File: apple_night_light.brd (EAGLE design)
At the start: 100 x 55 mm, 46 parts, among them Y1 16MHZ, Y2 16mhz

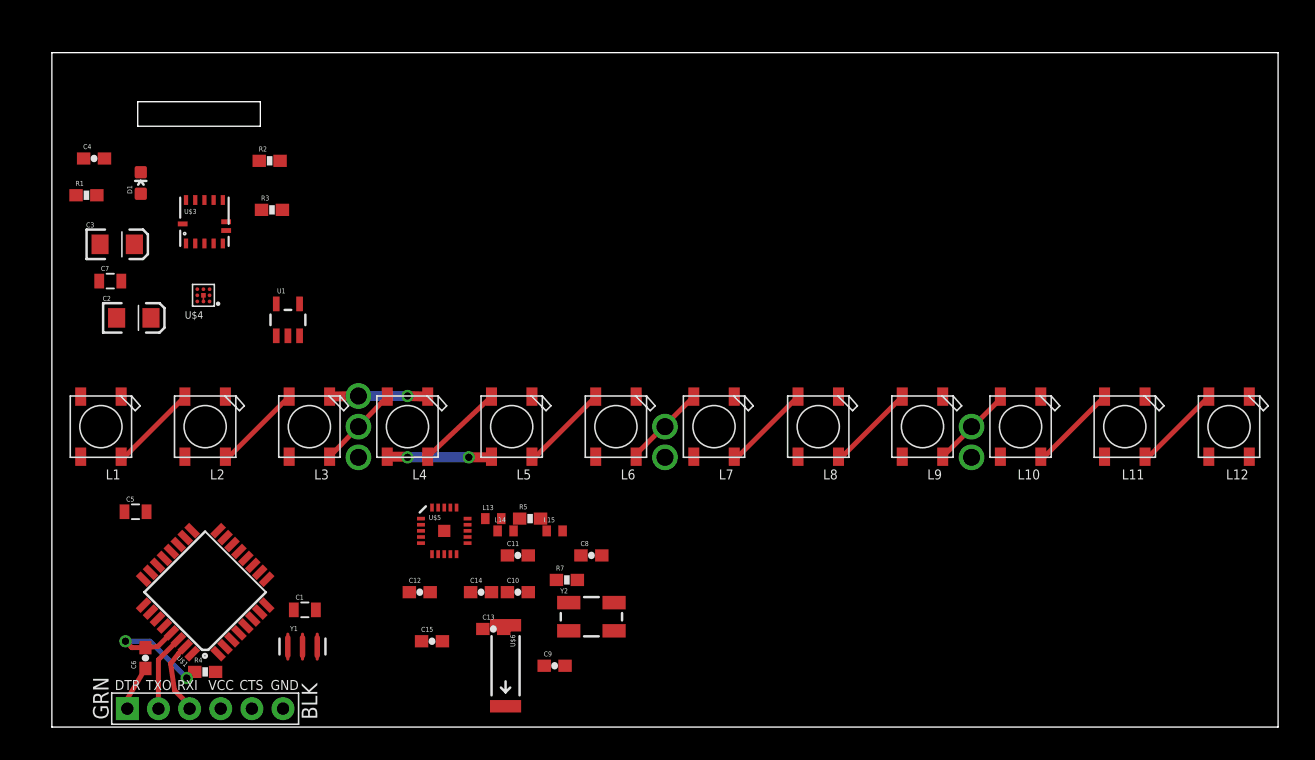
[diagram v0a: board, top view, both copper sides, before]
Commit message: some routing, adding current sensor, ground pours
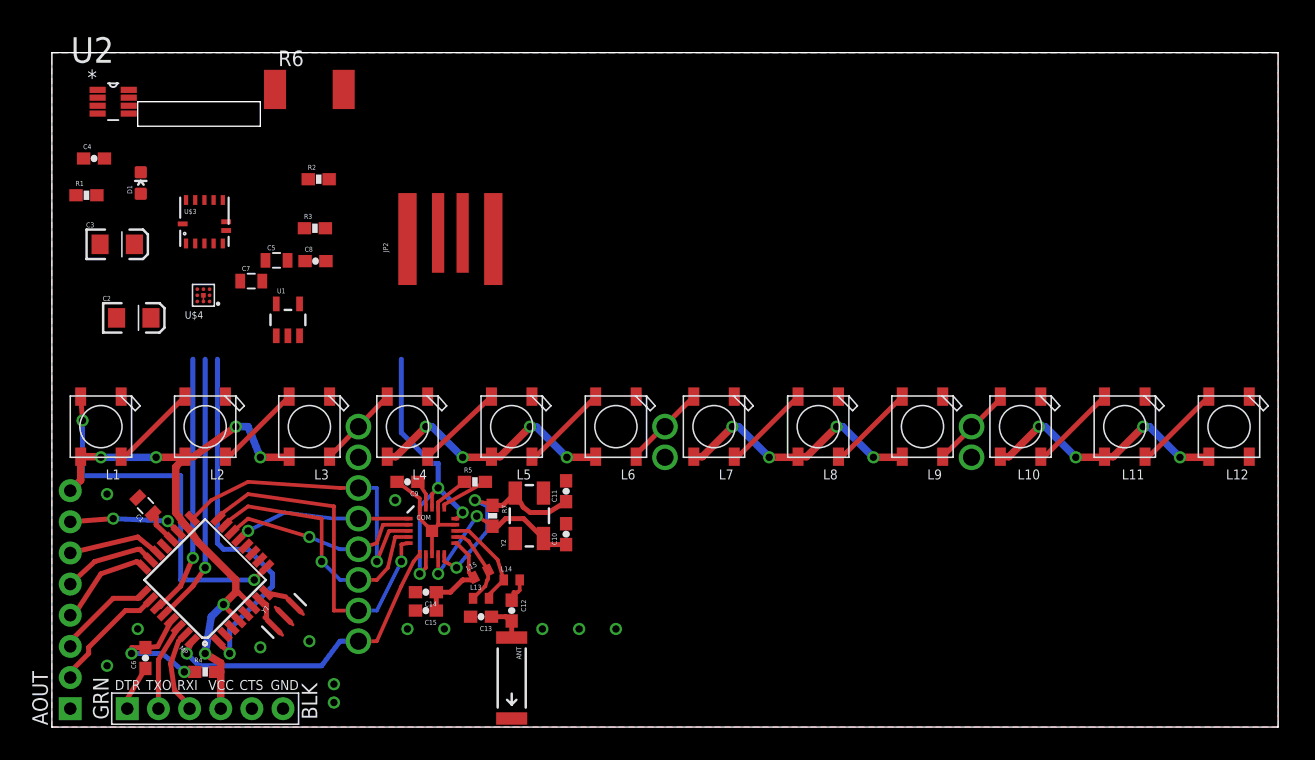
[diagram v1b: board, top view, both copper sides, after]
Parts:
- removed U$1: AVR-MEGA8-AI, SparkFun-DigitalIC:TQFP32-08
- removed U$5: NRF24L01SMD, SparkFun-RF:QFN20
- removed U$6: ANTENNA2SMD5, SparkFun-RF:ANTENNA-CHIP5
- added ANT: ANTENNA2SMD5, SparkFun-RF:ANTENNA-CHIP5
- added AOUT: (no value), SparkFun-Connectors:1X08_PIN1_NO_SILK
- added COM: NRF24L01SMD, SparkFun-RF:QFN20
- added JP2: USBPCB, SparkFun-Connectors:USB-A-PCB
- added MP: AVR-MEGA8-AI, SparkFun-DigitalIC:TQFP32-08
- added R6: 0.1/1% (PT2512FK-070R1L), SparkFun-Resistors:R2512
- added U2: INA219AIDCNR, Texas Instruments_By_element14_Batch_1:SOT65P280X145-8N
- moved C8 32.9 mm to (21.5, 38.0)
- moved C5 23.5 mm to (18.3, 38.1)
- moved C9 19.2 mm to (29.0, 20.0), turned to 180 degrees
- moved C1 15.5 mm to (7.63, 18.1), turned to 133.6 degrees
- moved C7 11.5 mm to (16.3, 36.4)
- moved Y2 9.66 mm to (38.9, 17.2), turned to 90 degrees
- moved R7 8.01 mm to (35.9, 17.2), turned to 270 degrees
- moved C12 7.65 mm to (37.5, 9.50), turned to 270 degrees
- moved L15 6.95 mm to (35.0, 12.5), turned to 26.5 degrees
- moved L13 6.58 mm to (35.0, 10.5)
- moved C11 6.55 mm to (41.9, 19.2), turned to 90 degrees
- moved C10 6.16 mm to (41.9, 15.7), turned to 90 degrees
- moved R5 5.41 mm to (34.5, 20.0)
- moved C14 4.50 mm to (30.5, 11.0), turned to 180 degrees
- moved R2 4.27 mm to (21.8, 44.7)
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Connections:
- removed net D5: U$1.9
- new net D4: MP.2
- net +3V3: now also COM.15, COM.18, COM.7; no longer R2.2, R3.2, U$5.15, U$5.18, U$5.7
- net +5V: now also AOUT.8, JP2.5V, MP.18, MP.4, MP.6, R2.2, R3.2, R6.2, U2.1, U2.4; no longer U$1.18, U$1.4, U$1.6
- net A0: now also AOUT.5, MP.23; no longer U$1.23
- net A1: now also AOUT.4, MP.24; no longer U$1.24
- net A2: now also AOUT.3, MP.25; no longer U$1.25
- net A3: now also AOUT.2, MP.26; no longer U$1.26
- net A6: now also AOUT.7, MP.19; no longer U$1.19
- net A7: now also AOUT.6, MP.22; no longer U$1.22
- net CE: now also COM.1, MP.13; no longer U$1.13, U$5.1
- net CSN: now also COM.2, MP.14; no longer U$1.14, U$5.2
- net D6: now also MP.10; no longer U$1.10
- net D7: now also MP.11; no longer U$1.11
- net D8: now also MP.12; no longer U$1.12
- net GND: now also AOUT.1, COM.0, COM.14, COM.17, COM.20, COM.8, JP2.GND, MP.21, MP.3, MP.5, R6.1, U2.2, U2.3; no longer U$1.21, U$1.3, U$1.5, U$5.0, U$5.14, U$5.17, U$5.20, U$5.8
- net IRQ: now also COM.6, MP.32; no longer U$1.32, U$5.6
- net MISO: now also COM.5, MP.16; no longer U$1.16, U$5.5
- net MOSI: now also COM.4, MP.15; no longer U$1.15, U$5.4
- net N$1: now also COM.11; no longer U$5.11
- net N$10: now also MP.7; no longer U$1.7
- net N$15: now also COM.19; no longer U$5.19
- net N$22: now also MP.29; no longer U$1.29
- net N$26: now also COM.13; no longer U$5.13
- net N$27: now also COM.9; no longer U$5.9
- net N$30: now also COM.10; no longer U$5.10
- net N$32: now also ANT.FEED; no longer U$6.FEED
- net N$6: now also COM.12; no longer U$5.12
- net N$7: now also MP.20; no longer U$1.20
- net N$8: now also COM.16; no longer U$5.16
- net N$9: now also MP.8; no longer U$1.8
- net NPIN: now also MP.9; no longer U$1.2
- net PROXINT: now also MP.1
- net RXI: now also MP.30; no longer U$1.30
- net SCK: now also COM.3, MP.17; no longer U$1.17, U$5.3
- net SCL: now also MP.28, U2.5; no longer U$1.28
- net SDA: now also MP.27, U2.6
- net TXO: now also MP.31; no longer U$1.31
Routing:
- net +5V: track 8.60 -> 114.5 mm, vias 2 -> 18
- net NPIN: track 0.00 -> 30.4 mm, vias 0 -> 2
- net PROXINT: track 0.00 -> 29.9 mm, vias 0 -> 1
- net MISO: track 0.00 -> 28.7 mm, vias 0 -> 2
- net +3V3: track 0.00 -> 26.9 mm, vias 0 -> 3
- net SCK: track 0.00 -> 26.3 mm, vias 0 -> 2
- net IRQ: track 0.00 -> 25.9 mm, vias 0 -> 2
- net MOSI: track 0.00 -> 22.2 mm, vias 0 -> 2
- net SCL: track 0.00 -> 22.1 mm, vias 0 -> 1
- net SDA: track 0.00 -> 21.3 mm, vias 0 -> 1
- net N$30: track 0.00 -> 18.3 mm, vias 0 -> 2
- net CSN: track 0.00 -> 16.4 mm, vias 0 -> 2
- net N$27: track 0.00 -> 16.0 mm, vias 0 -> 2
- net CE: track 0.00 -> 14.5 mm, vias 0 -> 2
- net A3: track 0.00 -> 9.74 mm
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- added copper zone on layer 1, net GND
- added copper zone on layer 16, net GND

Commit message: usb passthrough placed, better routing on neopixel power
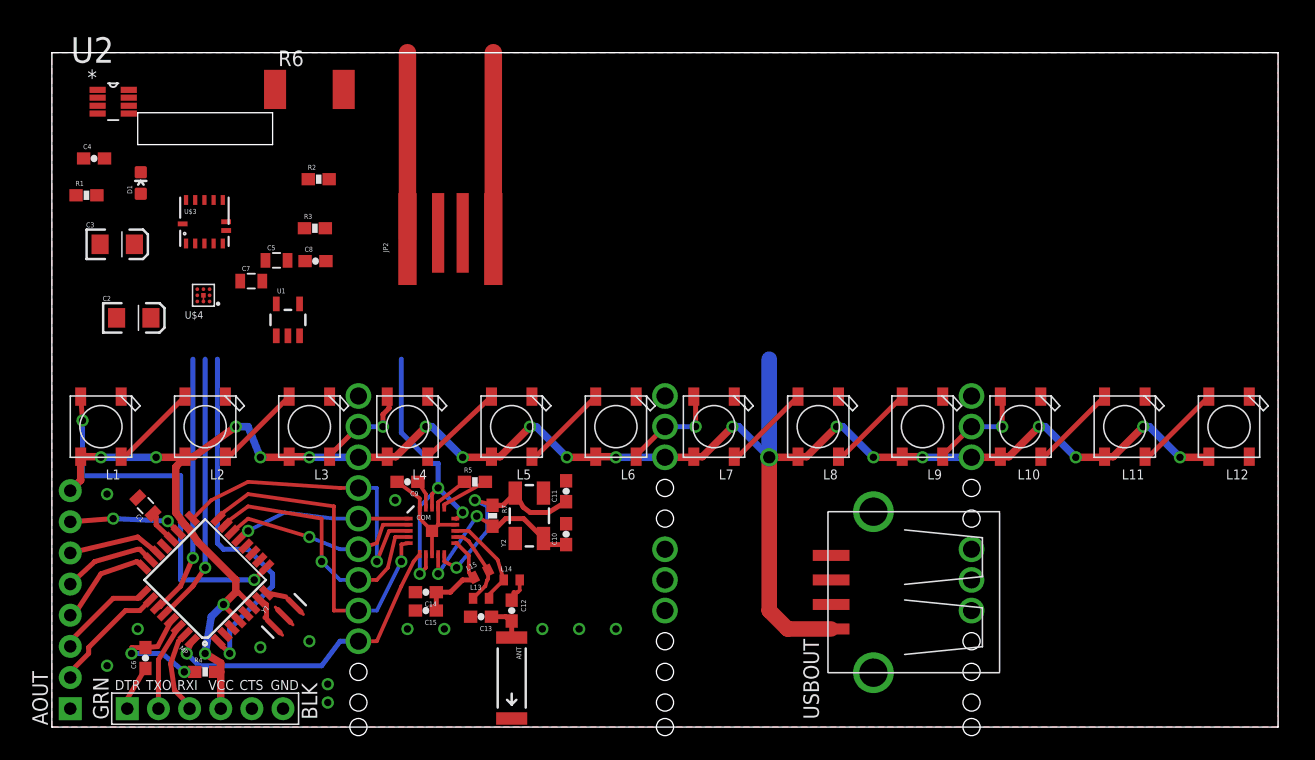
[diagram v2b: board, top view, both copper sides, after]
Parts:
- added USBOUT: USB-A-S, SparkFun-Connectors:USB-A-S
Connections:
- net +5V: now also USBOUT.VBUS
- net GND: now also USBOUT.GND
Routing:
- net +5V: track 114.5 -> 180.2 mm, vias 18 -> 24
- net GND: track 14.0 -> 29.2 mm, vias 13 -> 22
- net N$17: track 6.85 -> 8.64 mm, vias 0 -> 2
- net N$12: track 6.85 -> 8.49 mm, vias 0 -> 2
- net N$23: track 6.79 -> 8.14 mm, vias 0 -> 2
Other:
- outline, holes or cut-outs redrawn

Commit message: moved and corrected currentsensor, trying to fix clearances, adding temp/humidity sensor
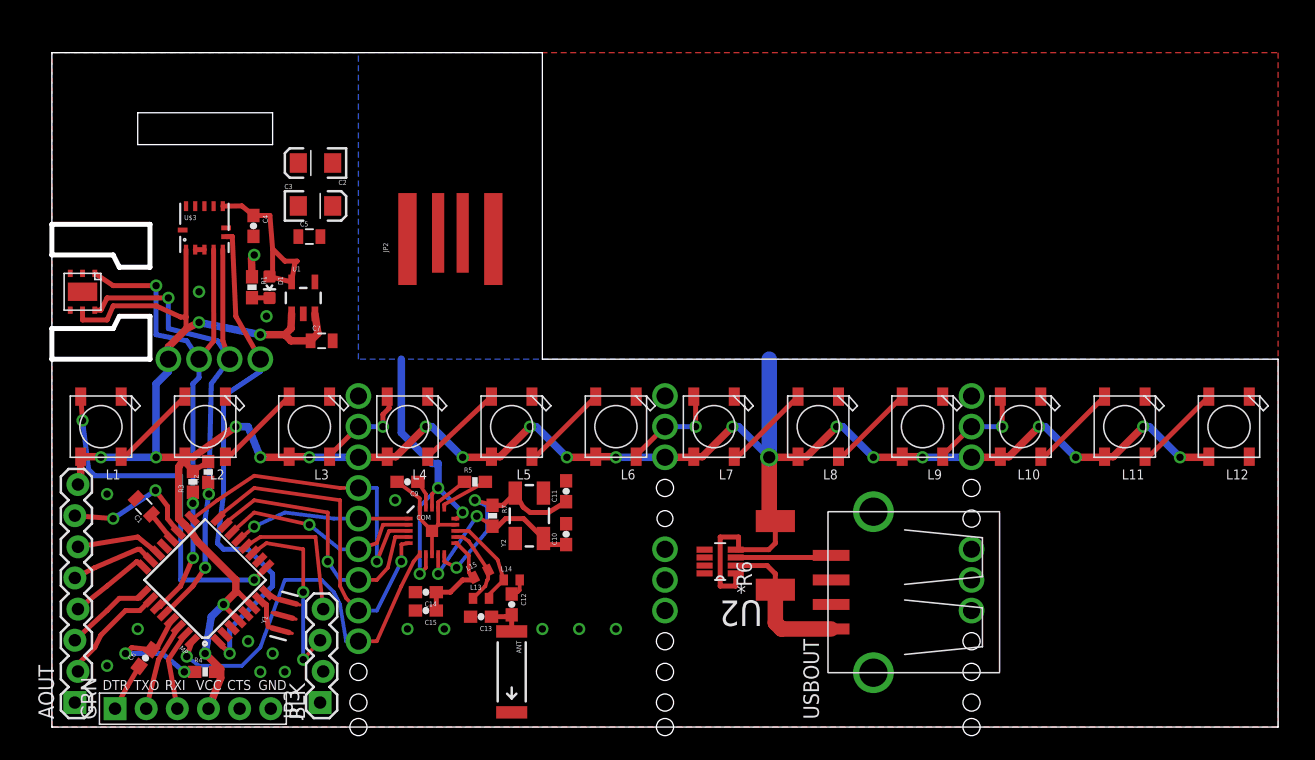
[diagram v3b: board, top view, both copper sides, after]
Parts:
- removed C8: 0.1uF, SparkFun-Capacitors:0603-CAP
- removed U$4: TMP006, SparkFun-DigitalIC:BGA8DS
- added JP3: (no value), SparkFun-Connectors:1X04_LOCK
- added U$1: SHT21, samuel:DFN6
- AOUT: device SparkFun-Connectors:1X08_PIN1_NO_SILK -> SparkFun-Connectors:1X08_LOCK
- moved U2 62.1 mm to (54.5, 13.5), turned to 180 degrees
- moved R6 53.7 mm to (59.0, 14.0), turned to 90 degrees
- moved R2 25.5 mm to (12.8, 20.8), turned to 90 degrees
- moved R3 22.9 mm to (11.5, 20.0), turned to 90 degrees
- moved C2 19.5 mm to (21.5, 46.0), turned to 180 degrees
- moved C3 16.5 mm to (21.5, 42.5)
- moved R1 15.4 mm to (16.3, 35.9), turned to 270 degrees
- moved C4 14.1 mm to (16.4, 40.9), turned to 270 degrees
- moved D1 13.5 mm to (17.8, 35.9), turned to 180 degrees
- moved C7 7.53 mm to (22.0, 31.5)
- moved C5 3.31 mm to (21.0, 40.0)
- moved U1 2.18 mm to (20.5, 35.0)
- moved JP1 1.00 mm to (11.5, 1.50)
- moved AOUT 0.71 mm to (2.00, 2.00)
- moved ANT 0.50 mm to (37.5, 4.50)
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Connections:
- new net V-: R6.1, U2.2, USBOUT.VBUS
- net +3V3: no longer C8.1
- net +5V: now also U$1.P$5; no longer U$4.A3, USBOUT.VBUS
- net D6: now also JP3.2
- net D7: now also JP3.3
- net D8: now also JP3.4
- net GND: now also JP3.1, U$1.P$2; no longer C8.2, R6.1, U$4.A1, U$4.A2, U$4.B1, U$4.C1, U2.2
- net SCL: now also U$1.P$6; no longer U$4.C3
- net SDA: now also U$1.P$1; no longer U$4.B3
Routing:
- net +5V: track 180.2 -> 212.1 mm, vias 24 -> 27
- net SCL: track 22.1 -> 47.6 mm, vias 1 -> 4
- net SDA: track 21.3 -> 45.4 mm, vias 1 -> 4
- net D7: track 0.00 -> 15.5 mm, vias 0 -> 2
- net +3V3: track 26.9 -> 42.2 mm
- net PROXINT: track 29.9 -> 42.5 mm, vias 1 -> 2
- net V-: track 0.00 -> 12.3 mm
- net D8: track 0.00 -> 11.8 mm
- net IRQ: track 25.9 -> 33.1 mm
- net GND: track 29.2 -> 23.8 mm, vias 22 -> 25
- net A6: track 9.22 -> 11.3 mm
- net N$29: track 0.00 -> 1.43 mm
- net A1: track 8.04 -> 6.90 mm
- net A2: track 8.04 -> 7.15 mm
- net MOSI: track 22.2 -> 23.1 mm
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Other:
- outline, holes or cut-outs redrawn

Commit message: before removing the nrf chip for breakout board
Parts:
- moved L14 0.50 mm to (37.5, 12.5)
- moved R4 0.50 mm to (13.0, 4.50)
- moved R7 0.07 mm to (36.0, 17.2)
- turned C2 to 0 degrees
- turned C3 to 180 degrees
- turned C6 to 75 degrees
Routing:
- net SDA: track 45.4 -> 90.0 mm, vias 4 -> 5
- net SCL: track 47.6 -> 91.6 mm, vias 4 -> 5
- net D6: track 0.00 -> 14.9 mm, vias 0 -> 2
- net +3V3: track 42.2 -> 45.3 mm
- net GND: track 23.8 -> 26.9 mm
- net IRQ: track 33.1 -> 34.3 mm
- net N$30: track 18.3 -> 17.6 mm
- net N$27: track 16.0 -> 15.4 mm
- net +5V: track 212.1 -> 212.7 mm
- net N$31: track 1.62 -> 2.12 mm

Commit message: more stuff, adding crypto board
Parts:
- removed ANT: ANTENNA2SMD5, SparkFun-RF:ANTENNA-CHIP5
- removed C10, C11: 22pf, SparkFun-Capacitors:0603-CAP
- removed C12: 1.5pF, SparkFun-Capacitors:0603-CAP
- removed C13: 1.0pf, SparkFun-Capacitors:0603-CAP
- removed C14: 4.7pf, SparkFun-Capacitors:0603-CAP
- removed C15: 2.2nf, SparkFun-Capacitors:0603-CAP
- removed C9: 0.1uF, SparkFun-Capacitors:0603-CAP
- removed COM: NRF24L01SMD, SparkFun-RF:QFN20
- removed JP3: (no value), SparkFun-Connectors:1X04_LOCK
- removed L13: 8.2nH, SparkFun-Passives:C0402
- removed L14: 3.9nH, SparkFun-Passives:C0402
- removed L15: 2.7nH, SparkFun-Passives:C0402
- removed R5, R7: 10K, SparkFun-Resistors:0603-RES
- removed Y2: 16mhz, SparkFun-FreqCtrl:CRYSTAL-SMD-5X3
- added DOUT: (no value), SparkFun-Connectors:1X04_LOCK
- added NRF: M04X2, SparkFun-Connectors:2X4
- added SPI: AVR_SPI_PRG_6NS, SparkFun-Connectors:2X3-NS
- added U3: ATSHA204-TSU, SparkFun-DigitalIC:SOT23-3
- moved C2 12.0 mm to (18.0, 34.5)
- moved C5 5.70 mm to (22.5, 34.5)
- moved U1 4.50 mm to (20.5, 39.5)
- moved D1 3.54 mm to (17.2, 39.4)
- moved R1 3.54 mm to (15.8, 39.4)
- moved C3 3.16 mm to (22.5, 45.5), turned to 270 degrees
- moved C4 2.55 mm to (15.9, 43.4), turned to 90 degrees
- moved JP2 2.50 mm to (34.0, 38.0)
- moved R2 2.01 mm to (14.8, 20.6), turned to 31.7 degrees
- moved C7 1.12 mm to (22.5, 32.5)
- moved R3 0.90 mm to (12.2, 20.5), turned to 45 degrees
- moved C1 0.71 mm to (8.00, 18.5), turned to 94.9 degrees
- moved AOUT 0.50 mm to (1.50, 2.00)
- moved JP1 0.50 mm to (12.0, 1.50)
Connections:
- removed net IR-: U$3.2, U$3.3
- removed net N$1: C14.1, C15.1, COM.11, L15.1
- removed net N$15: C9.1, COM.19
- removed net N$26: COM.13, L13.2, L14.1
- removed net N$27: C10.1, COM.9, R7.2, Y2.1
- removed net N$30: C11.1, COM.10, R7.1, Y2.3
- removed net N$31: C12.1, L14.2
- removed net N$32: ANT.FEED, C12.2, C13.1
- removed net N$6: COM.12, L13.1, L15.2
- removed net N$8: COM.16, R5.2
- net +3V3: now also NRF.2; no longer COM.15, COM.18, COM.7
- net +5V: now also SPI.2, U3.2
- net CE: now also NRF.3; no longer COM.1
- net CSN: now also NRF.4, SPI.5; no longer COM.2
- net D6: now also DOUT.2; no longer JP3.2
- net D7: now also DOUT.3; no longer JP3.3
- net D8: now also DOUT.4; no longer JP3.4
- net GND: now also DOUT.1, NRF.1, SPI.6, U$3.2, U$3.3, U3.3; no longer C10.2, C11.2, C13.2, C14.2, C15.2, C9.2, COM.0, COM.14, COM.17, COM.20, COM.8, JP3.1, R5.1
- net IRQ: now also NRF.8; no longer COM.6
- net MISO: now also NRF.7, SPI.1; no longer COM.5
- net MOSI: now also NRF.6, SPI.4; no longer COM.4
- net SCK: now also NRF.5, SPI.3; no longer COM.3
- net SDA: now also U3.1
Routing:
- net +5V: track 212.7 -> 291.4 mm, vias 27 -> 33
- net +3V3: track 45.3 -> 14.2 mm, vias 3 -> 0
- net CSN: track 16.9 -> 36.1 mm
- net N$30: track 17.6 -> 0.00 mm, vias 2 -> 1
- net N$27: track 15.4 -> 0.00 mm, vias 2 -> 1
- net SCK: track 26.5 -> 38.7 mm
- net MOSI: track 23.1 -> 34.5 mm
- net N$1: track 8.55 -> 0.00 mm
- net N$26: track 8.06 -> 0.00 mm, vias 0 -> 1
- net SDA: track 90.0 -> 97.5 mm, vias 5 -> 6
- net N$6: track 6.81 -> 0.00 mm, vias 0 -> 1
- net MISO: track 28.4 -> 35.0 mm, vias 2 -> 1
- net GND: track 26.9 -> 32.7 mm, vias 25 -> 33
- net N$8: track 4.17 -> 0.00 mm, vias 0 -> 1
- net A6: track 11.3 -> 15.1 mm
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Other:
- outline, holes or cut-outs redrawn
